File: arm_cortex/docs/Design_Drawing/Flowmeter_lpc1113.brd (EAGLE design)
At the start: 100 x 70 mm, 79 parts, among them IC2 OP07CN, IC5 OP07CN, U1 LPC1113FBD48/302,1, U2 LD1117S33CTR, U4 MAX232ACSE+, U5 MAX485CSA+, U6 7805TV, U7 MCP4921-E/P, U8 SP1490, X1 MKDSN1,5/3-5,08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

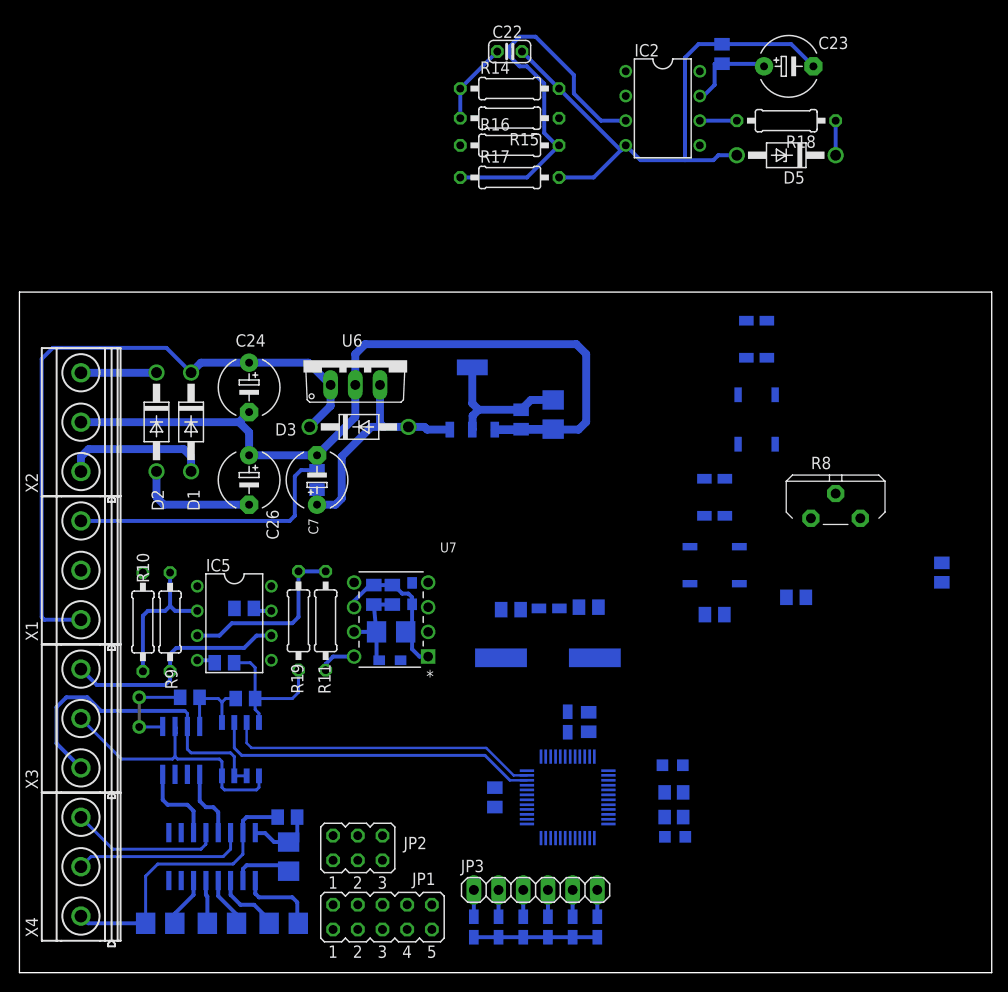
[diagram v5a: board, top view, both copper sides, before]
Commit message: 
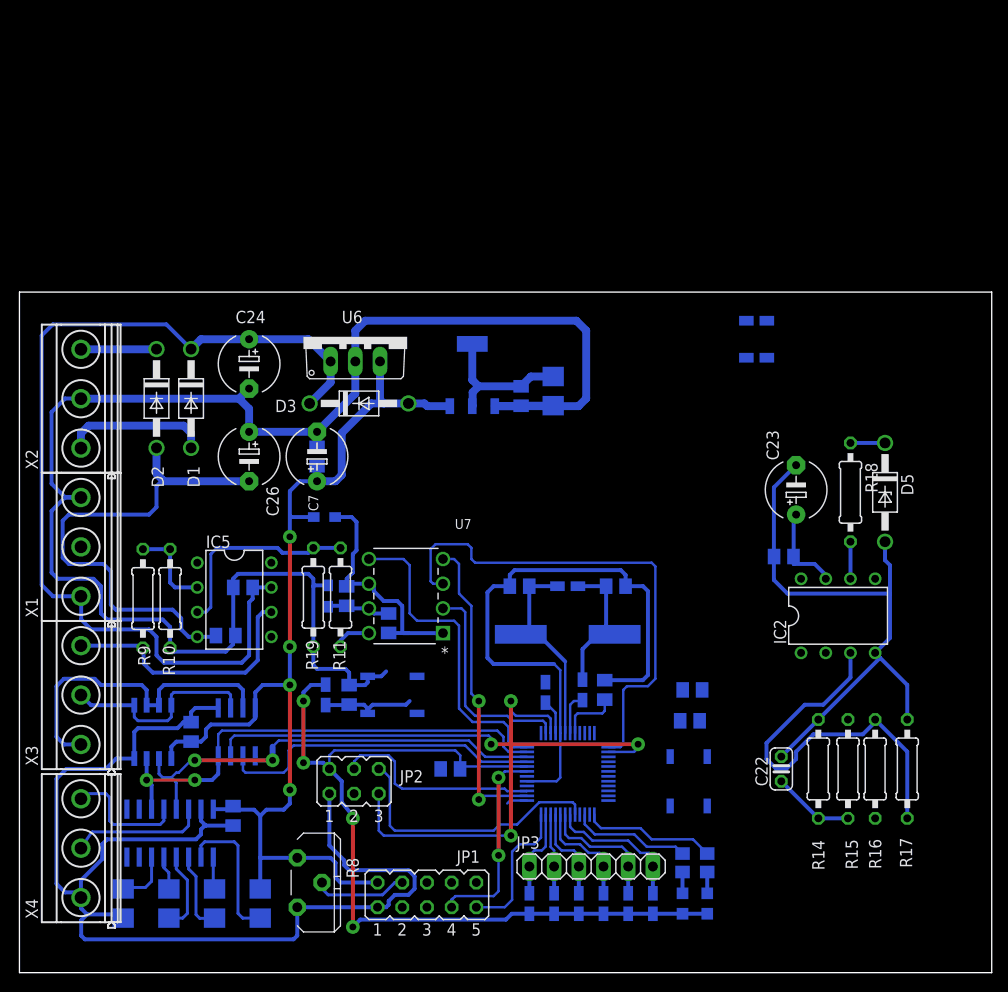
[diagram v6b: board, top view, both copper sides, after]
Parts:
- removed C28: 100n, rcl:C0805K
- removed C9: 10µ, rcl:CT3528
- moved C22 78.9 mm to (78.4, 21.0), turned to 90 degrees
- moved R14 76.8 mm to (82.2, 21.0), turned to 90 degrees
- moved R15 75.4 mm to (85.2, 21.0), turned to 270 degrees
- moved R16 74.3 mm to (88.0, 21.0), turned to 90 degrees
- moved R17 73.3 mm to (91.3, 21.0), turned to 90 degrees
- moved R8 66.5 mm to (29.8, 9.27), turned to 270 degrees
- moved IC2 55.2 mm to (84.2, 36.7), turned to 0 degrees
- moved C25 52.1 mm to (78.6, 42.8), turned to 0 degrees
- moved PRG_SW 47.0 mm to (38.4, 28.6), turned to 0 degrees
- moved R6 44.0 mm to (31.5, 28.6), turned to 90 degrees
- moved C23 43.6 mm to (79.9, 49.7), turned to 90 degrees
- moved R18 38.8 mm to (85.5, 49.4), turned to 270 degrees
- moved C6 38.5 mm to (33.9, 28.6), turned to 90 degrees
- moved D5 36.1 mm to (89.0, 49.4), turned to 270 degrees
- moved C8 28.3 mm to (69.2, 29.1), turned to 180 degrees
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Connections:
- removed net N$43: C11.2, C13.+, U2.2, U2.4
- net +12V: now also R15.1
- net 5V: no longer C28.2
- net GND: no longer C28.1
- net GND1: no longer C9.-
- net LCD_CONT: now also JP1.4; no longer JP1.10
- net LCD_D5: now also JP1.10; no longer JP1.4
- net LED1: now also U1.27; no longer U1.21
- net LED2: now also U1.25; no longer U1.20
- net N$11: no longer C9.+
- net N$27: no longer R15.1
- net RS485_RX_EN: now also U1.45; no longer U1.15
- net SWITCH0: now also U1.35
- net SWITCH1: now also U1.34
- net SWITCH2: now also U1.33
- net SWITCH3: now also U1.32
- net SWITCH4: now also U1.31
- net SWITCH5: now also U1.30
- net VCC: now also C11.2, C13.+, U2.2, U2.4
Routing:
- net GND: track 233.7 -> 422.4 mm, vias 2 -> 0
- net VCC: track 12.7 -> 111.9 mm, vias 0 -> 4
- net 5V: track 42.2 -> 112.0 mm, vias 0 -> 4
- net SPI1_SCK: track 0.00 -> 52.2 mm
- net RS485_TX_EN: track 0.00 -> 48.1 mm, vias 0 -> 2
- net /RESET: track 0.00 -> 38.4 mm, vias 0 -> 2
- net -12V: track 14.4 -> 51.5 mm
- net RS485_RX_EN: track 0.00 -> 33.7 mm
- net LDAC: track 0.00 -> 33.1 mm
- net SPI1_MOSI: track 0.00 -> 32.0 mm, vias 0 -> 2
- net +12V: track 70.4 -> 100.0 mm
- net SWDCLK: track 0.00 -> 28.1 mm
- net SPI1_CS: track 0.00 -> 22.1 mm
- net SWDIO: track 0.00 -> 21.6 mm
- net XTAL_IN: track 0.00 -> 21.0 mm
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
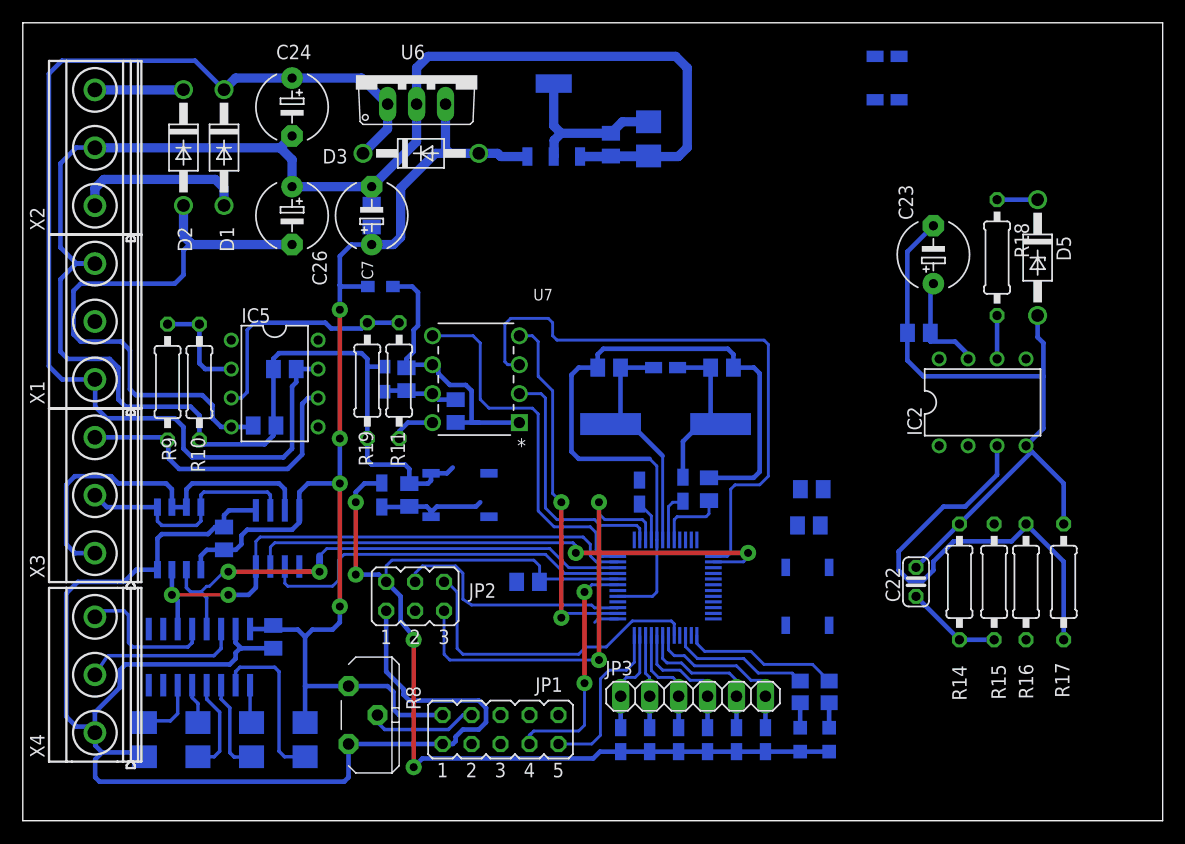
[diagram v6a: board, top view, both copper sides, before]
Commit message: single layer board
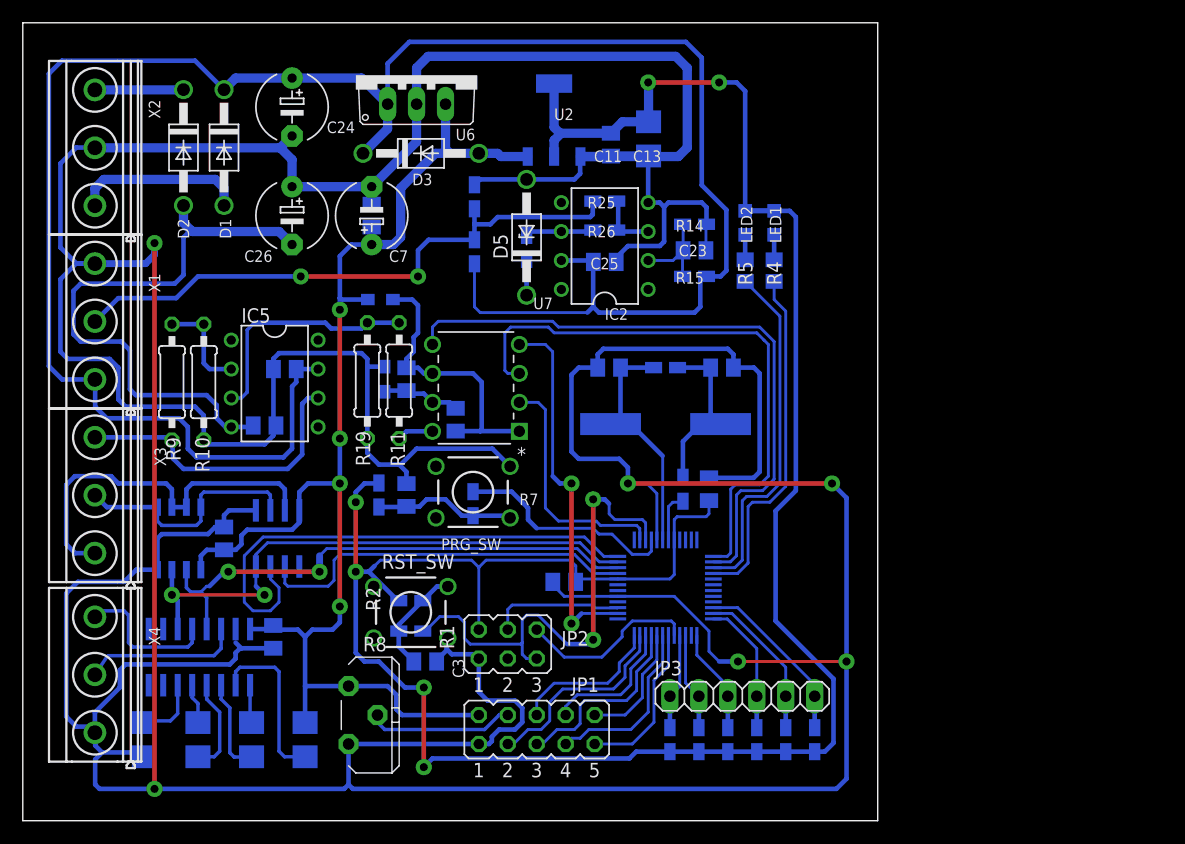
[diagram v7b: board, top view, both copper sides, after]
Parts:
- removed C22: 100n, rcl:C025-024X044
- removed C8: 100n, rcl:C0805K
- added R25: 10k, rcl:R0805W
- added R26: 22k, rcl:R0805W
- C23: value 100uF/60V -> 100n; device rcl:E5-6 -> rcl:C0805K
- PRG_SW, RST_SW: device SparkFun1:TACTILE_SWITCH_SMD -> SparkFun1:TACTILE-PTH
- R14, R15, R16, R17, R18: device rcl:0207/10 -> rcl:R0805W
- moved R2 63.5 mm to (34.0, 19.3), turned to 0 degrees
- moved R1 62.6 mm to (34.0, 16.6), turned to 0 degrees
- moved R17 61.7 mm to (39.6, 54.7), flipped to the bottom
- moved R16 56.4 mm to (39.6, 49.9), flipped to the bottom
- moved LED2 45.9 mm to (63.4, 52.5), turned to 180 degrees
- moved LED1 45.4 mm to (65.9, 52.5), turned to 180 degrees
- moved D5 44.9 mm to (44.2, 51.2), turned to 90 degrees
- moved R18 41.3 mm to (44.2, 50.3), flipped to the bottom, turned to 90 degrees
- moved R14 39.0 mm to (58.9, 52.3), flipped to the bottom, turned to 180 degrees
- moved R5 37.7 mm to (63.4, 48.3), turned to 270 degrees
- moved R15 37.5 mm to (58.9, 47.8), flipped to the bottom, turned to 0 degrees
- moved R4 37.0 mm to (65.9, 48.3), turned to 270 degrees
- moved IC2 35.9 mm to (51.1, 50.4), turned to 90 degrees
- moved C3 35.7 mm to (35.3, 14.0)
- moved RST_SW 34.8 mm to (34.0, 18.3), flipped to the top, turned to 0 degrees
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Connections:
- removed net N$22: C23.+, C25.1, IC2.7
- new net N$7: IC2.3, R25.2, R26.1
- net +12V: now also C25.1, IC2.7
- net 5V: no longer C8.1
- net GND: now also C23.2, RST_SW.4; no longer C22.2, C23.-, C8.2, RST_SW.2
- net LCD_D4: now also JP1.5, U1.33; no longer JP1.3, U1.1
- net LCD_D5: now also JP1.8, U1.34; no longer JP1.10, U1.11
- net LCD_D6: now also JP1.3, U1.35; no longer JP1.5, U1.12
- net LCD_D7: now also U1.36; no longer U1.24
- net LCD_EN: now also U1.31; no longer U1.43
- net LCD_R/W: now also JP1.10, U1.32; no longer JP1.8, U1.37
- net LCD_RS: now also U1.30; no longer U1.36
- net LDAC: now also U1.14; no longer U1.48
- net LED1: now also U1.16; no longer U1.27
- net LED2: now also U1.15; no longer U1.25
- net N$15: now also C23.1; no longer C22.1
- net N$37: now also R26.2
- net N$4: now also RST_SW.2; no longer RST_SW.4
- net RS485_TX_EN: now also U1.48; no longer U1.14
- net SENSOR_SIGNAL: now also R25.1; no longer IC2.3
- net SWITCH0: now also U1.28; no longer U1.35
- net SWITCH1: now also U1.27; no longer U1.34
- net SWITCH2: now also U1.25; no longer U1.33
- net SWITCH3: now also U1.24; no longer U1.32
- net SWITCH4: now also U1.23; no longer U1.31
- net SWITCH5: now also U1.22; no longer U1.30
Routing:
- net GND: track 422.4 -> 565.0 mm, vias 0 -> 6
- net VCC: track 111.9 -> 210.7 mm, vias 4 -> 6
- net +12V: track 100.0 -> 189.4 mm
- net LDAC: track 33.1 -> 56.0 mm
- net LED1: track 12.3 -> 30.8 mm
- net LCD_D6: track 0.13 -> 17.9 mm
- net LED2: track 13.7 -> 30.9 mm
- net LCD_D4: track 0.00 -> 17.0 mm
- net /BOOTLOADER: track 3.57 -> 19.6 mm
- net LCD_D7: track 0.00 -> 13.3 mm
- net SWDCLK: track 28.1 -> 15.8 mm
- net LCD_D5: track 0.00 -> 12.1 mm
- net SENSOR_SIGNAL: track 41.4 -> 52.2 mm, vias 0 -> 2
- net SWDIO: track 21.6 -> 11.7 mm
- net N$4: track 0.00 -> 9.47 mm
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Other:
- board size 100 x 70 mm -> 75 x 70 mm
